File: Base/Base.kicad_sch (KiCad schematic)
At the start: 6 parts, among them J1 USB_C_Receptacle_PowerOnly_6P, J2 Conn_01x04_Socket

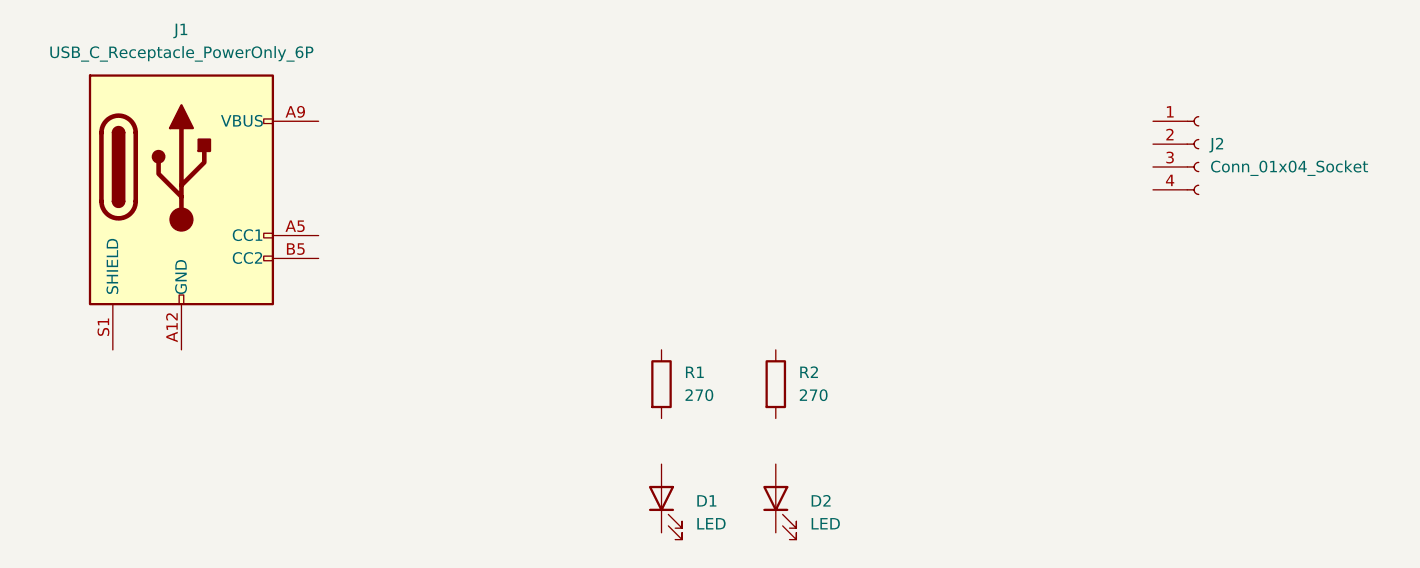
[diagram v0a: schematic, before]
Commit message: schematic update
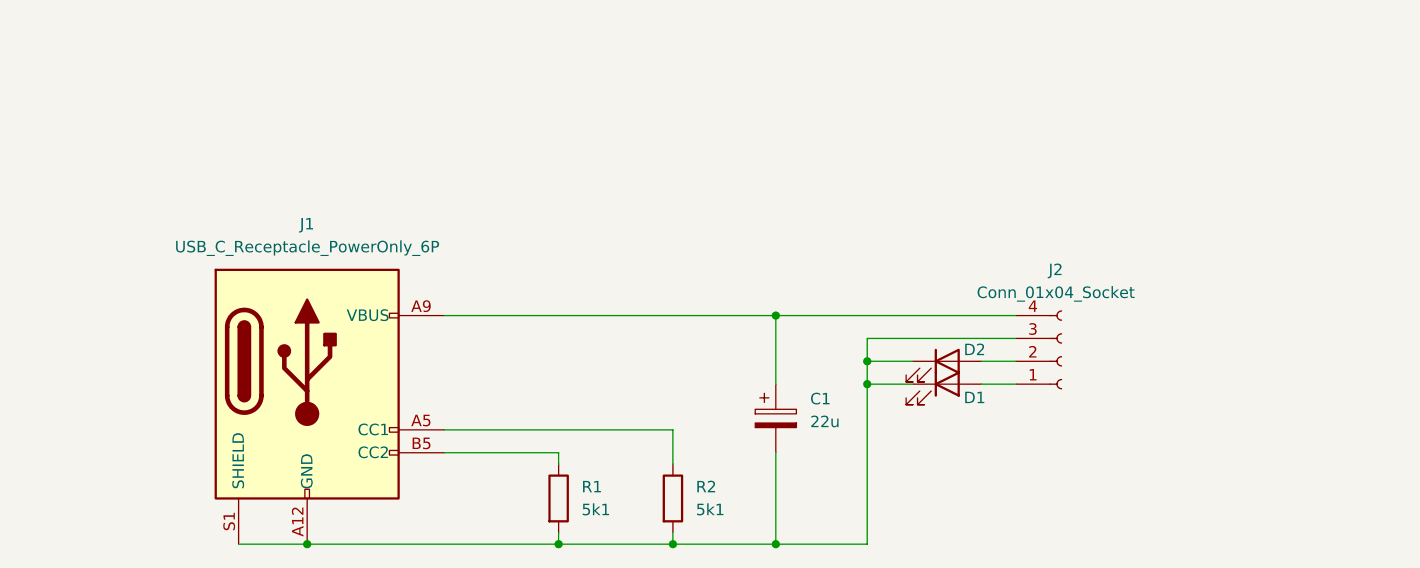
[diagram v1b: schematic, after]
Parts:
- added C1: 22u, Capacitor_THT:CP_Radial_D5.0mm_P2.50mm, symbol Device:C_Polarized
- R1, R2: value 270 -> 5k1
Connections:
- net at R2.1: now also J1.A5 (CC1)
- net at R2.2: now also D1.1 (K), D2.1 (K), J1.A12 (GND), J1.B12 (GND), J1.S1 (SHIELD), J2.3 (Pin_3), R1.2, C1.2
- net at R1.1: now also J1.B5 (CC2)
- net at D1.2 (A): now also J2.1 (Pin_1)
- net at D2.2 (A): now also J2.2 (Pin_2)
- net at J2.4 (Pin_4): now also J1.A9 (VBUS), J1.B9 (VBUS), C1.1
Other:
- moved on the sheet: D1, D2, J1, J2, R1, R2

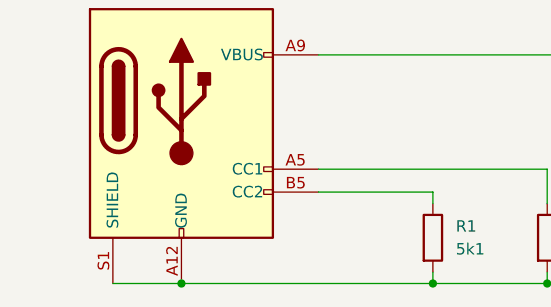
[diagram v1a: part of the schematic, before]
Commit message: RC2, un-ground shield
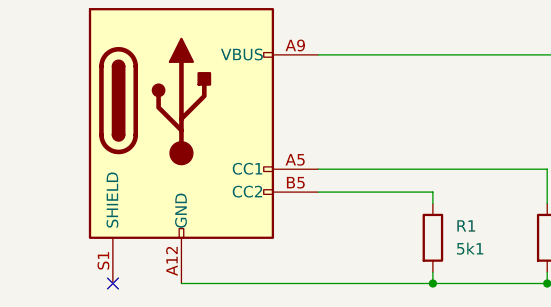
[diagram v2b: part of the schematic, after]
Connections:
- net at C1.2, D1.1 (K), D2.1 (K)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: no longer J1.S1 (SHIELD)
- no-connect marks 0 -> 1
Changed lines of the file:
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@@
 	(paper "A4")
-	(junction
-		(at 113.03 110.49)
-		(diameter 0)
-		(color 0 0 0 0)
-	)
 	(junction
 		(at 153.67 110.49)
@@
 		(diameter 0)
 		(color 0 0 0 0)
+	)
+	(no_connect
+		(at 105.41 110.49)
 	)
 	(wire
@@
 		)
 		(stroke
-			(width 0)
-			(type default)
-		)
-	)
-	(wire
-		(pts
-			(xy 113.03 110.49) (xy 105.41 110.49)
-		)
-		(stroke
